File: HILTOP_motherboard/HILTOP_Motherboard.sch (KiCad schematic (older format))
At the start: 118 parts, among them J10 HDMI, J11 DISP_PWR, J12 DISPLAY_PORT, J14 PROG_PWR2, J15 PROG_PWR1, J16 SOFT_START_PWR, J17 PWR_LED, J18 RS232_DEBUG, J19 Micro_SD_Card, J2 ATX_MOLEX_02X12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

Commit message: Added new USB2.0 device
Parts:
- removed C1, C13, C21: 10uF, Capacitors_SMD:C_0805, symbol C
- removed C15, C2, C20: 100nF, Capacitors_SMD:C_0603, symbol C
- removed D2, D3, D4: Red LED, LEDs:LED_0603, symbol LED
- removed J6: USB_A, KiCAD_PCB_Lib:USB_A_Vertical_Lumberg_2410_01, symbol USB_A-RESCUE-ProdRETTester
- removed J7: USB_HEADER, Pin_Headers:Pin_Header_Straight_2x05_Pitch2.54mm, symbol USB_HEADER
- removed R2, R3, R4: 1K, Resistors_SMD:R_0603, symbol R
- added R? (x2): 4K7, Resistors_SMD:R_0603, symbol R
- R122: value 3K3 -> 1K5; Devtank 101-013 -> 101-032
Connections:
- net labels added: BACKPLANE_USB_N, BACKPLANE_USB_P, SATA_USB_N, SATA_USB_P
- wire segments 773 -> 724
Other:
- moved on the sheet: C24, C25, C3, C5, J11, J12, J14, J15, J8, R10, R11, R119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

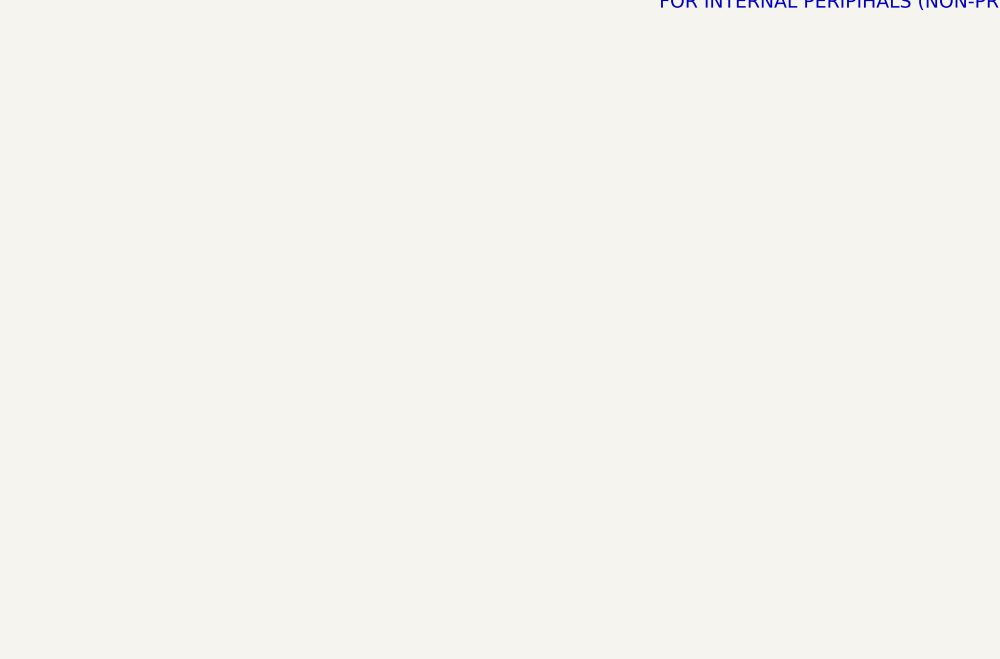
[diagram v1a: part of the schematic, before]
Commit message: Added RTC and Temp Sensor
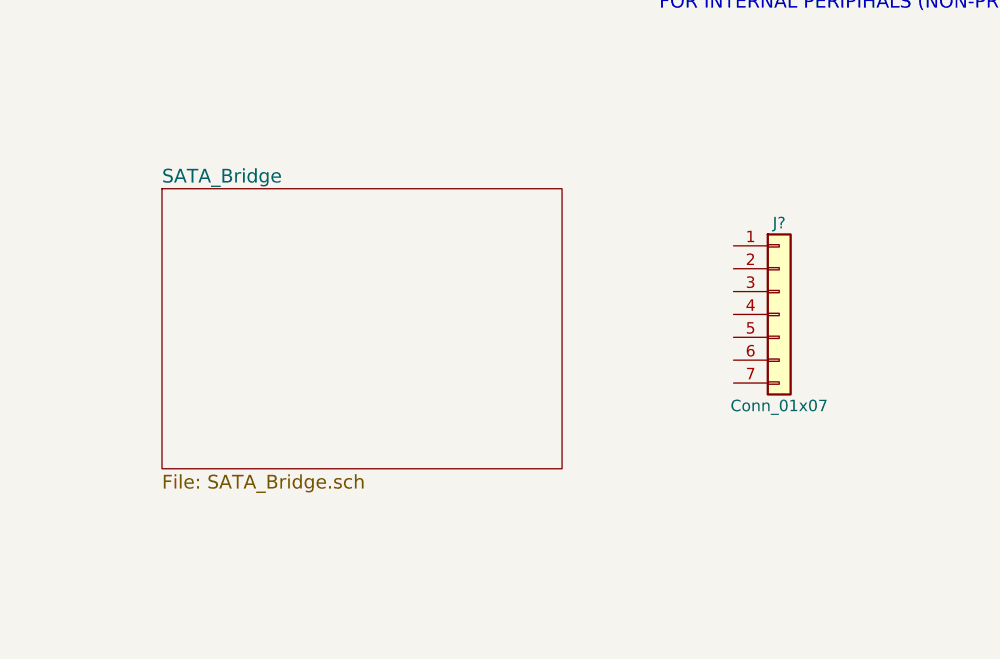
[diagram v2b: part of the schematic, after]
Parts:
- added J?: Conn_01x07, symbol Conn_01x07
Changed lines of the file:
@@
 EESchema Schematic File Version 2
+LIBS:HILTOP_Motherboard-rescue
 LIBS:Devtank
 LIBS:Zilog
@@
 $Descr A2 23386 16535
 encoding utf-8
-Sheet 1 9
+Sheet 1 10
 Title "HILTOP Motherboard"
 Date "26th January 2018"
@@
 Text Label 5375 4500 2    60   ~ 0
 BACKPLANE_USB_N
+$Sheet
+S 2475 5600 1750 1225
+U 5A951BF0
+F0 "SATA_Bridge" 60
+F1 "SATA_Bridge.sch" 60
+$EndSheet
+$Comp
+L Conn_01x07 J?
+U 1 1 5A956DE4
+P 5175 6150
+F 0 "J?" H 5175 6550 50  0000 C CNN
+F 1 "Conn_01x07" H 5175 5750 50  0000 C CNN
+F 2 "" H 5175 6150 50  0001 C CNN
+F 3 "" H 5175 6150 50  0001 C CNN
+	1    5175 6150
+	1    0    0    -1
+$EndComp
 $EndSCHEMATC

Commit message: Added more detail for SATA bridge chip circuit
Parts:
- added J?: EXT_FAN, symbol Conn_01x03
- J?: value Conn_01x07 -> SATA
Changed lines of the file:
@@
 $Descr A2 23386 16535
 encoding utf-8
-Sheet 1 10
+Sheet 1 11
 Title "HILTOP Motherboard"
 Date "26th January 2018"
@@
 P 5175 6150
 F 0 "J?" H 5175 6550 50  0000 C CNN
-F 1 "Conn_01x07" H 5175 5750 50  0000 C CNN
+F 1 "SATA" H 5175 5750 50  0000 C CNN
 F 2 "" H 5175 6150 50  0001 C CNN
 F 3 "" H 5175 6150 50  0001 C CNN
@@
 	1    0    0    -1
 $EndComp
+$Comp
+L Conn_01x03 J?
+U 1 1 5A95FB4B
+P 21300 4150
+F 0 "J?" H 21300 4350 50  0000 C CNN
+F 1 "EXT_FAN" H 21300 3950 50  0000 C CNN
+F 2 "" H 21300 4150 50  0001 C CNN
+F 3 "" H 21300 4150 50  0001 C CNN
+	1    21300 4150
+	1    0    0    -1
+$EndComp
+$Sheet
+S 5525 7300 1750 3525
+U 5A96D361
+F0 "BackPlane" 60
+F1 "BackPlane.sch" 60
+$EndSheet
 $EndSCHEMATC

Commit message: Fixed giabit LAN Schematic errors
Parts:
- removed C18, C7: 10uF, Capacitors_SMD:C_0805, symbol C
- removed J3: USB_A, KiCAD_PCB_Lib:USB_A_Vertical_Lumberg_2410_01, symbol USB_A-RESCUE-ProdRETTester
- added C18, C7, C? (x2): 100uF, Capacitor_SMD:CP_Elec_6.3x7.7, symbol CP
- added C?: 100nF, Capacitor_SMD:C_1210_3225Metric, symbol C
- added J?: USB Front Panel, Connector_Molex:Molex_Picoflex_90325-0008_2x04_P1.27mm_Vertical, symbol Conn_01x08
- C19, C5: footprint Capacitors_SMD:C_0603 -> Capacitor_SMD:C_0603_1608Metric
- C3: value 10uF -> 100uF; footprint Capacitors_SMD:C_0805 -> Capacitor_SMD:CP_Elec_6.3x7.7; symbol C -> CP; Devtank 105-001 -> 108-002
- R148: value 0R -> 330R
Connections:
- net labels added: FR_PANEL_USB_N, FR_PANEL_USB_P, FR_PANEL_USB_PWR, PWR_LED_A, PWR_SW, TR0_N, TR0_P, TR1_N, TR1_P, TR2_N, TR2_P, TR3_N, TR3_P
- wire segments 724 -> 884
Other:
- moved on the sheet: C19, C5, C8, J4, J?

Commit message: Added more detail to motherboard schemas
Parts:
- removed J8: RS485_CONN, Connectors:IDC_Header_Straight_12pins, symbol CONN_02X06
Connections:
- net labels added: ADJ_DC
- net labels removed: RET_DC, RET_GND
- wire segments 884 -> 700
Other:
- moved on the sheet: J?, R10, R11, R153, R154, R155, R156, R8, R82, R9

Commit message: Finished CAN nd RS485 interface circuits
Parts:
- removed C66, C68, C70: 100nF, Capacitors_SMD:C_0603, symbol C
- removed R153, R154, R155, R156: 0R, Resistors_SMD:R_0603, symbol R
- added C? (x2): 100nF, Capacitor_SMD:C_0603_1608Metric, symbol C
- added J?: Conn_02x08_Odd_Even, symbol Conn_02x08_Odd_Even
- added J?: Conn_02x05_Odd_Even, symbol Conn_02x05_Odd_Even
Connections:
- net +12V: no longer EXP1.39 (P39), EXP1.40 (P40)
- net +3V3: now also EXP1.3 (P3), EXP1.4 (P4); no longer EXP1.7 (P7), EXP1.8 (P8)
- net -5V: no longer EXP1.3 (P3), EXP1.4 (P4), EXP2.3 (P3), EXP2.4 (P4), EXP3.3 (P3), EXP3.4 (P4)
- net GND: now also C?.2, C?.2, J?.10 (Pin_10), J?.15 (Pin_15), J?.16 (Pin_16), J?.7 (Pin_7), J?.8 (Pin_8), J?.9 (Pin_9)
- net PR_GPIO1: now also EXP1.12 (P12)
- net SYS_PWM1: no longer EXP1.12 (P12)
- net Ethernet/CT renamed CT
- net Ethernet/LEDG_K renamed LEDG_K
- net Ethernet/LEDY_K renamed LEDY_K
- new net +5V_ISO1: J?.1 (Pin_1)
- new net +5V_ISO2: J?.5 (Pin_5)
- new net +5V_ISO3: C?.1, J?.1 (Pin_1)
- new net +5V_ISO4: C?.1, J?.9 (Pin_9)
- new net A1: J?.2 (Pin_2)
- new net A2: J?.10 (Pin_10)
- new net B1: J?.3 (Pin_3)
- new net B2: J?.11 (Pin_11)
- new net CAN1_H: J?.2 (Pin_2)
- new net CAN1_L: J?.3 (Pin_3)
- new net CAN2_H: J?.6 (Pin_6)
- new net CAN2_L: J?.7 (Pin_7)
- new net GND_ISO1: J?.4 (Pin_4)
- new net GND_ISO2: J?.8 (Pin_8)
- new net GND_ISO3: J?.6 (Pin_6)
- new net GND_ISO4: J?.14 (Pin_14)
- new net Y1: J?.5 (Pin_5)
- new net Y2: J?.13 (Pin_13)
- new net Z1: J?.4 (Pin_4)
- new net Z2: J?.12 (Pin_12)
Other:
- note added: "Gigabit Ethernet"
- note added: "Isolated CAN-FD Ports"
- note added: "Isolated RS485 Ports"
- note added: "USB 2.0 Ports for External Periphals (Protected)"
- note removed: "FOR EXTERNAL PERIPIHALS (PROTECTED)"
- note removed: "FOR INTERNAL PERIPIHALS (NON-PROTECTED)"
- moved on the sheet: C18, C19, C3, C5, C53, C55, C59, C7, C8, C?, J4, J9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

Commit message: Updated pinouts for Backplane and Compute Module
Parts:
- removed C23, C98: 100nF, Capacitors_SMD:C_0603, symbol C
- removed J18: RS232_DEBUG, Connectors_Samtec:SL-104-X-XX_1x04, symbol CONN_01X04
- removed J5: SYSTEM_SPI_I2C, Connectors:IDC_Header_Straight_12pins, symbol CONN_02X06
- added J?: USB_B, symbol USB_B
- added J?: EXT_TEMP_MON, symbol Conn_01x03
- added J?: CAMERA_PORT, KiCAD_PCB_Lib:DSI_SFW15R-2STE1LF, symbol CONN_01X15
- added Q?: ZXMN6A07F, symbol Q_NMOS_GSD
- added R? (x4): DNF, Resistors_SMD:R_0603, symbol R
- added R? (x2): 0R, Resistors_SMD:R_0603, symbol R
- added R? (x2): 470R, Resistors_SMD:R_0603, symbol R
- added R? (x2): 10K, Resistors_SMD:R_0603, symbol R
- J?: symbol Conn_01x03 -> Conn_01x04
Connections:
- net BoardPower/PWR_SW is gone; now on net PWR_SW: J16.2 (P2)
- net PWR_LED_A is gone; now on net +5V: J?.8 (Pin_8)
- net +12V: now also J?.2 (Pin_2)
- net +3V3: now also J?.1 (Pin_1), J?.15 (P15), R?.1
- net Earth: now also J?.5 (Shield)
- net GND: now also J?.1 (P1), J?.10 (P10), J?.3 (Pin_3), J?.4 (GND), J?.4 (P4), J?.7 (P7), Q?.2 (S), R?.2
- net PWR_ENABLE: no longer R8.1
- net SYS_PWM1: now also R?.1
- net at J?.1 (Pin_1): now also Q?.3 (D)
- net FAN_SENSE: now reaches J?.3 (Pin_3)
- net FAN_SENSE: now also R?.2
- net PWR_LED renamed BCK_SHUTDOWN
- net Processor/DISP1_CK_N renamed DISP1_CK_N
- net Processor/DISP1_CK_P renamed DISP1_CK_P
- net Processor/DISP1_D0_N renamed DISP1_D0_N
- net Processor/DISP1_D0_P renamed DISP1_D0_P
- net Processor/DISP1_D1_N renamed DISP1_D1_N
- net Processor/DISP1_D1_P renamed DISP1_D1_P
- net Processor/PI_SCL0_DISP renamed I2C0_SCL
- net I2C0_SCL: now also R15.2; no longer R?.2
- net Processor/PI_SDA0_DISP renamed I2C0_SDA
- net I2C0_SDA: now also R13.2; no longer R?.2
- net RETPower/VMON_1 renamed AdjPower/VMON_1
- net RETPower/VMON_2 renamed AdjPower/VMON_2
- net SYS_SCL renamed I2C1_SCL
- net I2C1_SCL: now also R?.2, J?.13 (P13); no longer R15.2
- net SYS_SDA renamed I2C1_SDA
- net I2C1_SDA: now also R?.2, J?.14 (P14); no longer R13.2
- net ice40_FPGA/PWR_LED: no longer names the net of R9.2
- new net: J?.4 (Pin_4), R?.1
- new net: Q?.1 (G), R?.1, R?.1
- new net: R?.1, R?.1, R?.2
- new net CAM1_CK_N: J?.8 (P8)
- new net CAM1_CK_P: J?.9 (P9)
- new net CAM1_D0_N: J?.2 (P2)
- new net CAM1_D0_P: J?.3 (P3)
- new net CAM1_D1_N: J?.5 (P5)
- new net CAM1_D1_P: J?.6 (P6)
- new net CAM1_IO0: J?.11 (P11), R?.2
- new net CAM1_IO1: J?.12 (P12), R?.2
- new net DC_OUT_ENABLE: R8.1
- new net EXT_TEMP_1WIRE: J?.2 (Pin_2)
- new net Processor/PI_GPIO13_PWM1: R?.2, R?.2
- new net SPI1_CS1_CAM_IO0: R?.1
- new net SPI1_CS2_CAM_IO1: R?.1
- new net SYS_FAN_DC: R?.2
- new net SYS_FAN_PWM: R?.1, R?.2, R?.2
- new net USB_Debug/USB_N: J?.2 (D-)
- new net USB_Debug/USB_P: J?.3 (D+)
- no-connect marks 0 -> 1
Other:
- note added: "Front Panel - PWR Sw. & Indication"
- moved on the sheet: C22, C24, C25, C26, C27, C51, C53, C55, C59, EXP1, EXP2, EXP3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

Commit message: Furthe progress on Schematics, assigned all main footprints using latest libraries, removed unwanted tracking and parts from original PCB layout
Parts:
- added J1, J24: Conn_02x10_Odd_Even, Connector_PinHeader_2.54mm:PinHeader_2x10_P2.54mm_Vertical, symbol Conn_02x10_Odd_Even
- C10, C119, C4, C6: footprint Capacitors_SMD:CP_Elec_6.3x5.3 -> Capacitor_SMD:CP_Elec_6.3x5.3
- C11, C120, C16, C9: footprint Capacitors_SMD:CP_Elec_5x5.3 -> Capacitor_SMD:CP_Elec_5x5.3
- C12, C121, C14, C17, C22, C24, C25, C26, C59, C71, C72, C73, C74, C75, C8: footprint Capacitors_SMD:C_0603 -> Capacitor_SMD:C_0603_1608Metric
- C27, C50: footprint Capacitors_SMD:C_0805 -> Capacitor_SMD:C_0805_2012Metric
- C51, C53, C55, C77: footprint Capacitors_SMD:C_0603 -> Capacitor_SMD:C_0201_0603Metric
- D1: footprint LEDs:LED_0603 -> LED_SMD:LED_0603_1608Metric
- EXP1, EXP2, EXP3: footprint Connectors:IDC_Header_Straight_40pins -> Connector_PinHeader_2.54mm:PinHeader_2x20_P2.54mm_Vertical
- J10: footprint KiCAD_PCB_Lib:FCI_10029449-11RLF -> Devtank_PCB_Lib:FCI_10029449-11RLF
- J11: footprint Connectors_Molex:Molex_KK-6410-05_05x2.54mm_Straight -> Connector_Molex:Molex_KK-254_AE-6410-05A_1x05_P2.54mm_Vertical
- J12: footprint KiCAD_PCB_Lib:DSI_SFW15R-2STE1LF -> Devtank_PCB_Lib:DSI_SFW15R-2STE1LF
- J18: renamed from J?; footprint (none) -> Connector_USB:USB_B_Horizontal
- J19: footprint KiCAD_PCB_Lib:uSD_47219-2001 -> Devtank_PCB_Lib:uSD_MSDC-PP03; Devtank 705-001 -> 705-002
- J20: renamed from J?; footprint KiCAD_PCB_Lib:DSI_SFW15R-2STE1LF -> Devtank_PCB_Lib:DSI_SFW15R-2STE1LF
- J21: renamed from J?; footprint (none) -> Connector_Molex:Molex_KK-254_AE-6410-04A_1x04_P2.54mm_Vertical
- J3: renamed from J?; footprint (none) -> Connector:SATA-7_THT_VERT_1; Devtank (none) -> 716-001
- J4: footprint KiCAD_PCB_Lib:USB_A_Double_Lumberg_2410_03 -> Devtank_PCB_Lib:USB_A_Double_Lumberg_2410_03
- J6: renamed from J?; footprint (none) -> Connector_Molex:Molex_Picoflex_90325-0010_2x05_P1.27mm_Vertical
- J7: renamed from J?; footprint (none) -> Connector_Molex:Molex_Picoflex_90325-0016_2x08_P1.27mm_Vertical
- J8: renamed from J?; footprint (none) -> Connector_Molex:Molex_KK-254_AE-6410-03A_1x03_P2.54mm_Vertical
- J9: footprint KiCAD_PCB_Lib:RJ45_TRANSFO_STEWART -> Devtank_PCB_Lib:RJ45_TRANSFO_STEWART
- L1, L2, L3, L8: footprint KiCAD_PCB_Lib:Inductor_8x8 -> Devtank_PCB_Lib:Inductor_8x8
- Q5: renamed from Q?; footprint (none) -> Package_TO_SOT_SMD:SOT-23
- R1, R10, R11, R119, R12, R120, R121, R122, R124, R125, R13, R14, R15, R16, R17, R54, R6, R8, R82, R83, R85, R9: footprint Resistors_SMD:R_0603 -> Resistor_SMD:R_0603_1608Metric
- R148, R149, R150, R151: footprint Resistors_SMD:R_1210 -> Resistor_SMD:R_1210_3225Metric
- R18, R19, R2, R22, R23, R24, R25, R26, R28, R29, R3, R4: renamed from R?; footprint Resistors_SMD:R_0603 -> Resistor_SMD:R_0603_1608Metric
- R5, R56, R7: footprint Resistors_SMD:R_1206 -> Resistor_SMD:R_1206_3216Metric
- TP10, TP11, TP12, TP13, TP14, TP8, TP9: footprint Measurement_Points:Measurement_Point_Round-TH_Small -> TestPoint:TestPoint_THTPad_D1.5mm_Drill0.7mm
- U1: footprint TO_SOT_Packages_SMD:SOT-23-6 -> Package_TO_SOT_SMD:SOT-23-6
- U25: footprint TO_SOT_Packages_SMD:SOT-23-6 -> Package_TO_SOT_SMD:TSOT-23-6
- gave numbers to parts that had none: 6
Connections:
- net PR_GPIO2 is gone; now on net PR_GPIO22: EXP1.15 (P15)
- net PR_GPIO3 is gone; now on net PR_GPIO23: EXP1.16 (P16)
- net PR_GPIO4 is gone; now on net +3V3: EXP1.17 (P17)
- net PR_GPIO5 is gone; now on net SPI0_MOSI: EXP1.19 (P19)
- net PR_GPIO6 is gone; now on net GND: EXP1.20 (P20)
- net PR_GPIO7 is gone; now on net SPI0_MISO: EXP1.21 (P21)
- net PR_GPIO8 is gone; now on net PR_GPIO25: EXP1.22 (P22)
- net +3V3: now also EXP1.1 (P1); no longer EXP1.3 (P3), EXP1.4 (P4)
- net +5V: now also EXP1.4 (P4); no longer EXP1.1 (P1)
- net DEBUG_RX: now also EXP1.10 (P10)
- net DEBUG_TX: now also EXP1.8 (P8)
- net FP_GPIO_1: no longer EXP1.24 (P24)
- net FP_GPIO_10: no longer EXP1.35 (P35)
- net FP_GPIO_11: no longer EXP1.36 (P36)
- net FP_GPIO_2: no longer EXP1.25 (P25)
- net FP_GPIO_3: no longer EXP1.26 (P26)
- net FP_GPIO_4: no longer EXP1.27 (P27)
- net FP_GPIO_5: no longer EXP1.29 (P29)
- net FP_GPIO_6: no longer EXP1.30 (P30)
- net FP_GPIO_7: no longer EXP1.31 (P31)
- net FP_GPIO_8: no longer EXP1.32 (P32)
- net FP_GPIO_9: no longer EXP1.34 (P34)
- net GND: now also EXP1.14 (P14), EXP1.25 (P25), EXP1.30 (P30), EXP1.34 (P34), EXP1.39 (P39); no longer EXP1.11 (P11), EXP1.13 (P13), EXP1.18 (P18), EXP1.23 (P23), EXP1.28 (P28), EXP1.33 (P33), EXP1.37 (P37), EXP1.38 (P38), EXP1.5 (P5)
- net I2C0_SCL: now also EXP1.28 (P28)
- net I2C0_SDA: now also EXP1.27 (P27)
- net I2C1_SCL: now also EXP1.5 (P5)
- net I2C1_SDA: now also EXP1.3 (P3)
- net PR_GPIO24: now also EXP1.18 (P18)
- net PR_GPIO26: now also EXP1.37 (P37)
- net PR_GPIO27: now also EXP1.13 (P13)
- net SPI0_CS0: now also EXP1.24 (P24)
- net SPI0_CS1: now also EXP1.26 (P26)
- net SPI0_SCLK: now also EXP1.23 (P23)
- net SPI1_CS0: now also EXP1.12 (P12)
- net SPI1_CS1_CAM_IO0: now also EXP1.11 (P11)
- net SPI1_CS2_CAM_IO1: now also EXP1.36 (P36)
- net SPI1_MISO: now also EXP1.35 (P35)
- net SPI1_MOSI: now also EXP1.38 (P38)
- net SPI1_SCLK: now also EXP1.40 (P40)
- net SYS_CLK0: now also EXP1.7 (P7)
- net SYS_CLK1: now also EXP1.29 (P29); no longer EXP1.10 (P10)
- net SYS_PWM0: now also EXP1.32 (P32)
- net SYS_PWM1: now also EXP1.33 (P33)
- net SYS_TRIG: now also EXP1.31 (P31)
- removed net PR_GPIO1: EXP1.12 (P12), EXP1.14 (P14)
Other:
- moved on the sheet: EXP2, EXP3
